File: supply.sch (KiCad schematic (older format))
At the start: 65 parts, among them IC1 TPS54561, J10 61300311121, J3 DC_SOCKET, U4 TPS65296, U5 TPS62823DLCT

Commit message: Replace 5R1 resistor and clean up
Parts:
- removed R41: R_5R1_1020, lpddr4-test-board-footprints:1020-res, symbol lpddr4-test-board:R_5R1_1020
- added R35: R_5R1_0402, antmicro-footprints:0402-res, symbol antmicroResistors0402:R_5R1_0402
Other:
- note added: "Decoupling"
- moved on the sheet: C165, C167, C170, C172, C174, C175, C178, C180, C182, C183, C27, C28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

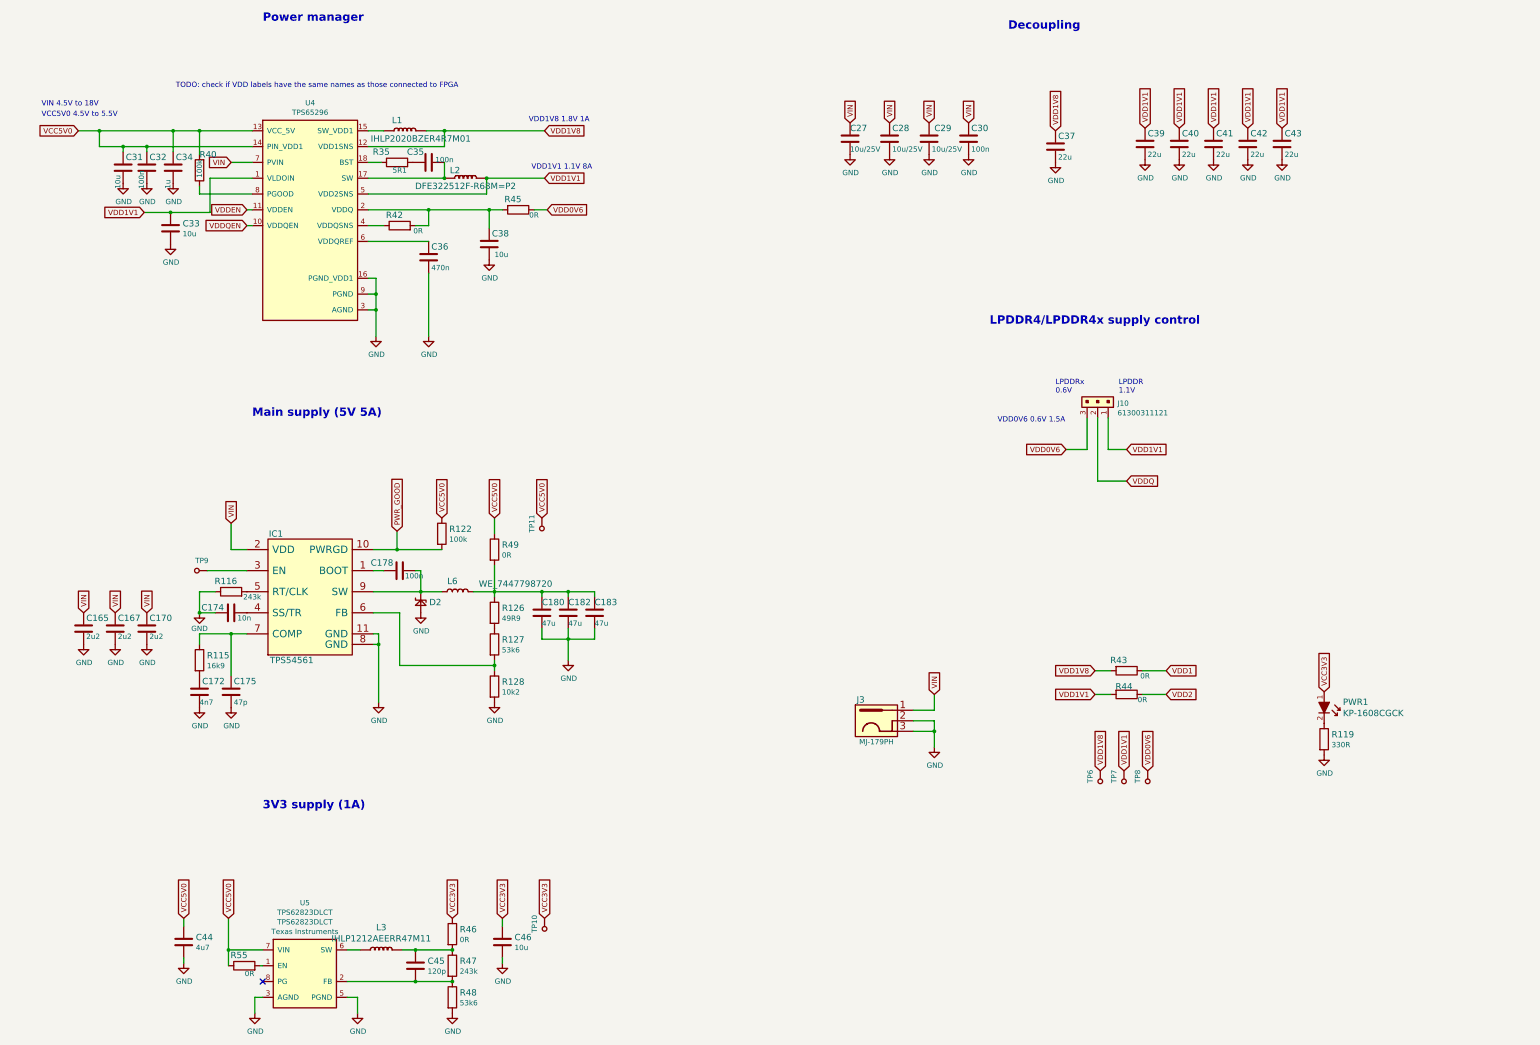
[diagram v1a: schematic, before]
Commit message: Clean up schematic
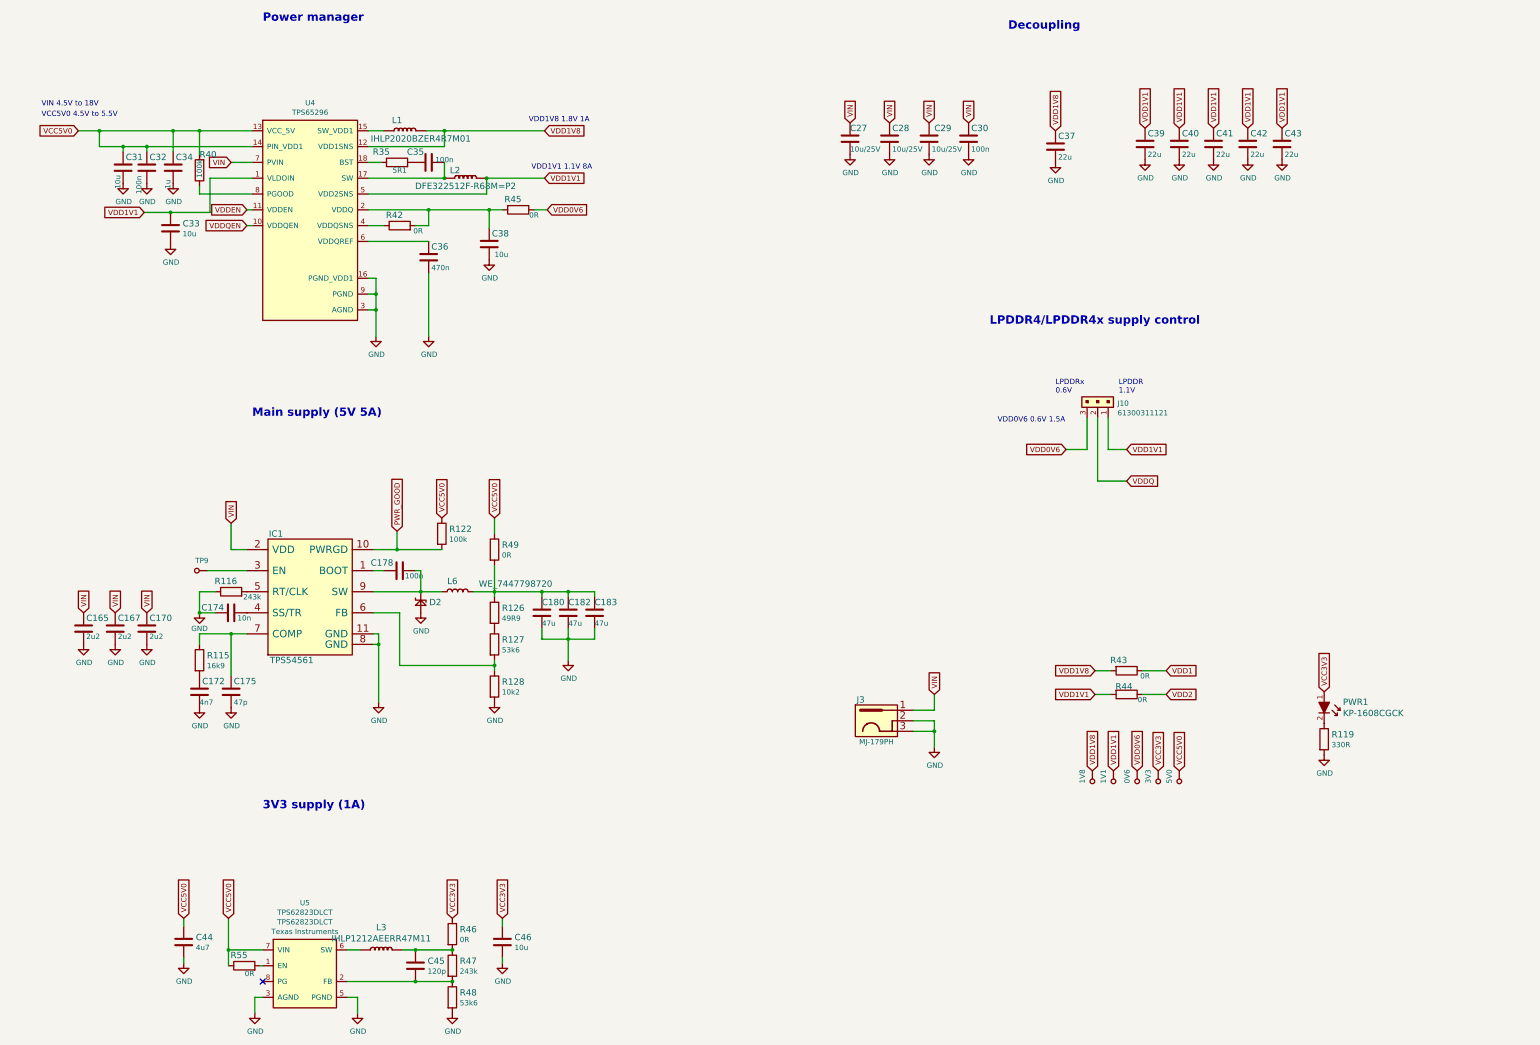
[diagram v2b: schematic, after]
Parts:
- renumbered TP8 to 0V6, TP7 to 1V1, TP6 to 1V8, TP10 to 3V3, TP11 to 5V0
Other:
- note removed: "TODO: check if VDD labels have the same names as those connected to FPGA"
- moved on the sheet: 0V6, 1V1, 1V8, 3V3, 5V0
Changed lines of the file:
@@
 F 4 "Walsin" H 2650 2750 60  0001 L CNN "Manufacturer"
 F 5 "0402X104K6R3CT" H 2650 2650 60  0001 L CNN "MPN"
-F 6 "100n" V 2400 2150 50  0000 L CNN "Val"
+F 6 "100n" V 2375 2100 50  0000 L CNN "Val"
 	1    2450 2350
 	1    0    0    -1
@@
 Wire Wire Line
 	4450 10225 4450 10375
-Text Notes 2725 1600 0    50   ~ 0
-TODO: check if VDD labels have the same names as those connected to FPGA
 $Comp
 L lpddr4-test-board:IHLP1212AEERR47M11 L3
@@
 	0    1    1    0
 $EndComp
-Text GLabel 6200 5675 1    50   Input ~ 0
+Text GLabel 12250 8075 1    50   Input ~ 0
 VCC5V0
 $Comp
-L lpddr4-test-board:TP_SMD1MM TP11
+L lpddr4-test-board:TP_SMD1MM 5V0
 U 1 1 60212554
-P 6200 5775
-F 0 "TP11" V 6105 5822 50  0000 C CNN
-F 1 "TP_SMD1MM" H 6200 5675 50  0001 C CNN
-F 2 "lpddr4-test-board-footprints:Testpoint_smd_1mm" H 6400 5975 60  0001 L CNN
-F 3 "" H 6400 6075 60  0001 L CNN
-	1    6200 5775
+P 12250 8175
+F 0 "5V0" V 12155 8222 50  0000 C CNN
+F 1 "TP_SMD1MM" H 12250 8075 50  0001 C CNN
+F 2 "lpddr4-test-board-footprints:Testpoint_smd_1mm" H 12450 8375 60  0001 L CNN
+F 3 "" H 12450 8475 60  0001 L CNN
+	1    12250 8175
 	1    0    0    -1
 $EndComp
@@
 Wire Wire Line
 	5825 9850 5825 9900
-Text GLabel 6225 9475 1    50   Input ~ 0
+Text GLabel 12050 8075 1    50   Input ~ 0
 VCC3V3
 $Comp
-L lpddr4-test-board:TP_SMD1MM TP10
+L lpddr4-test-board:TP_SMD1MM 3V3
 U 1 1 6026C4D0
-P 6225 9575
-F 0 "TP10" V 6130 9622 50  0000 C CNN
-F 1 "TP_SMD1MM" H 6225 9475 50  0001 C CNN
-F 2 "lpddr4-test-board-footprints:Testpoint_smd_1mm" H 6425 9775 60  0001 L CNN
-F 3 "" H 6425 9875 60  0001 L CNN
-	1    6225 9575
+P 12050 8175
+F 0 "3V3" V 11955 8222 50  0000 C CNN
+F 1 "TP_SMD1MM" H 12050 8075 50  0001 C CNN
+F 2 "lpddr4-test-board-footprints:Testpoint_smd_1mm" H 12250 8375 60  0001 L CNN
+F 3 "" H 12250 8475 60  0001 L CNN
+	1    12050 8175
 	1    0    0    -1
 $EndComp
@@
 	-1   0    0    1
 $EndComp
-Text GLabel 11950 8075 1    50   Input ~ 0
+Text GLabel 11850 8075 1    50   Input ~ 0
 VDD0V6
 $Comp
-L lpddr4-test-board:TP_SMD1MM TP6
+L lpddr4-test-board:TP_SMD1MM 1V8
 U 1 1 602C0646
-P 11500 8175
-F 0 "TP6" V 11405 8222 50  0000 C CNN
-F 1 "TP_SMD1MM" H 11500 8075 50  0001 C CNN
-F 2 "lpddr4-test-board-footprints:Testpoint_smd_1mm" H 11700 8375 60  0001 L CNN
-F 3 "" H 11700 8475 60  0001 L CNN
-	1    11500 8175
-	1    0    0    -1
-$EndComp
-$Comp
-L lpddr4-test-board:TP_SMD1MM TP7
+P 11425 8175
+F 0 "1V8" V 11330 8222 50  0000 C CNN
+F 1 "TP_SMD1MM" H 11425 8075 50  0001 C CNN
+F 2 "lpddr4-test-board-footprints:Testpoint_smd_1mm" H 11625 8375 60  0001 L CNN
+F 3 "" H 11625 8475 60  0001 L CNN
+	1    11425 8175
+	1    0    0    -1
+$EndComp
+$Comp
+L lpddr4-test-board:TP_SMD1MM 1V1
 U 1 1 602C252D
-P 11725 8175
-F 0 "TP7" V 11630 8222 50  0000 C CNN
-F 1 "TP_SMD1MM" H 11725 8075 50  0001 C CNN
-F 2 "lpddr4-test-board-footprints:Testpoint_smd_1mm" H 11925 8375 60  0001 L CNN
-F 3 "" H 11925 8475 60  0001 L CNN
-	1    11725 8175
-	1    0    0    -1
-$EndComp
-$Comp
-L lpddr4-test-board:TP_SMD1MM TP8
+P 11625 8175
+F 0 "1V1" V 11530 8222 50  0000 C CNN
+F 1 "TP_SMD1MM" H 11625 8075 50  0001 C CNN
+F 2 "lpddr4-test-board-footprints:Testpoint_smd_1mm" H 11825 8375 60  0001 L CNN
+F 3 "" H 11825 8475 60  0001 L CNN
+	1    11625 8175
+	1    0    0    -1
+$EndComp
+$Comp
+L lpddr4-test-board:TP_SMD1MM 0V6
 U 1 1 602C27EC
-P 11950 8175
-F 0 "TP8" V 11855 8222 50  0000 C CNN
-F 1 "TP_SMD1MM" H 11950 8075 50  0001 C CNN
-F 2 "lpddr4-test-board-footprints:Testpoint_smd_1mm" H 12150 8375 60  0001 L CNN
-F 3 "" H 12150 8475 60  0001 L CNN
-	1    11950 8175
+P 11850 8175
+F 0 "0V6" V 11755 8222 50  0000 C CNN
+F 1 "TP_SMD1MM" H 11850 8075 50  0001 C CNN
+F 2 "lpddr4-test-board-footprints:Testpoint_smd_1mm" H 12050 8375 60  0001 L CNN
+F 3 "" H 12050 8475 60  0001 L CNN
+	1    11850 8175
 	1    0    0    -1
 $EndComp
@@
 Wire Wire Line
 	5675 2450 6225 2450
-Text GLabel 11725 8075 1    50   Input ~ 0
+Text GLabel 11625 8075 1    50   Input ~ 0
 VDD1V1
-Text GLabel 11500 8075 1    50   Input ~ 0
+Text GLabel 11425 8075 1    50   Input ~ 0
 VDD1V8
 Text GLabel 11450 7125 0    50   Input ~ 0

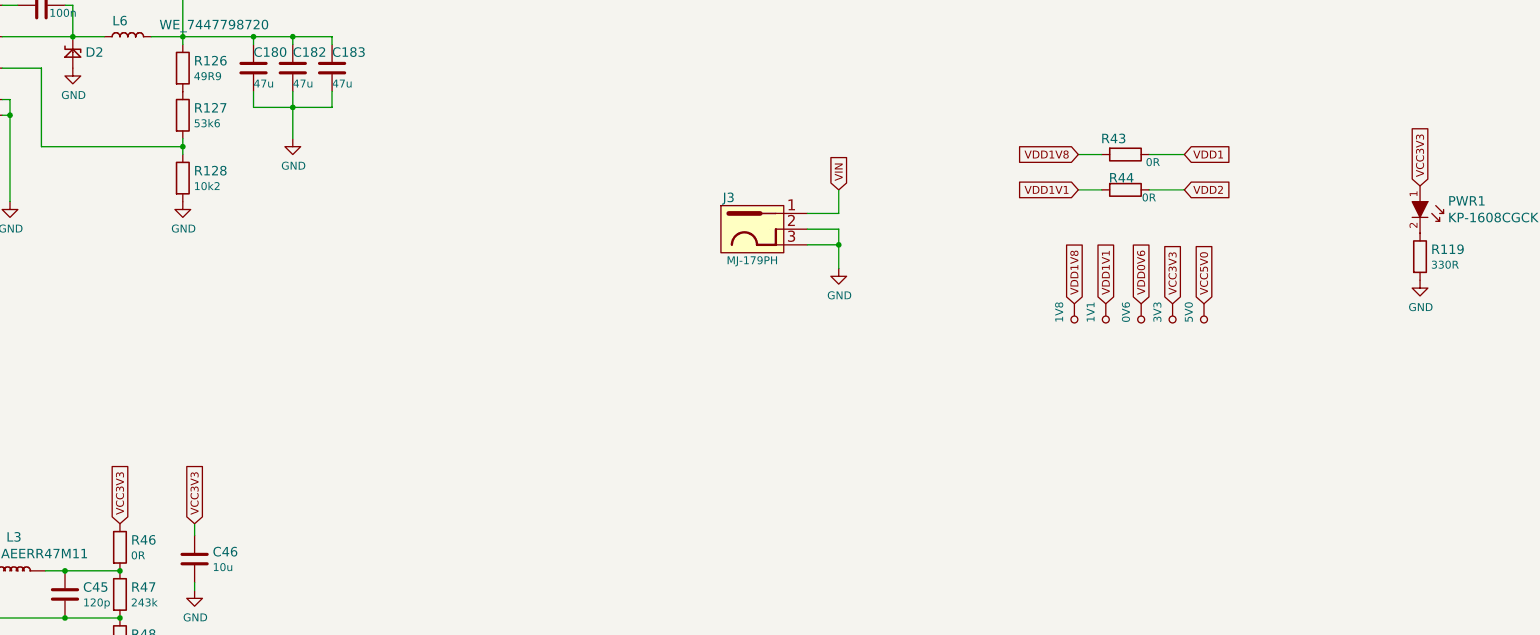
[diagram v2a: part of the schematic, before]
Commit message: Replace VCC3V3 with 3V3_SYS
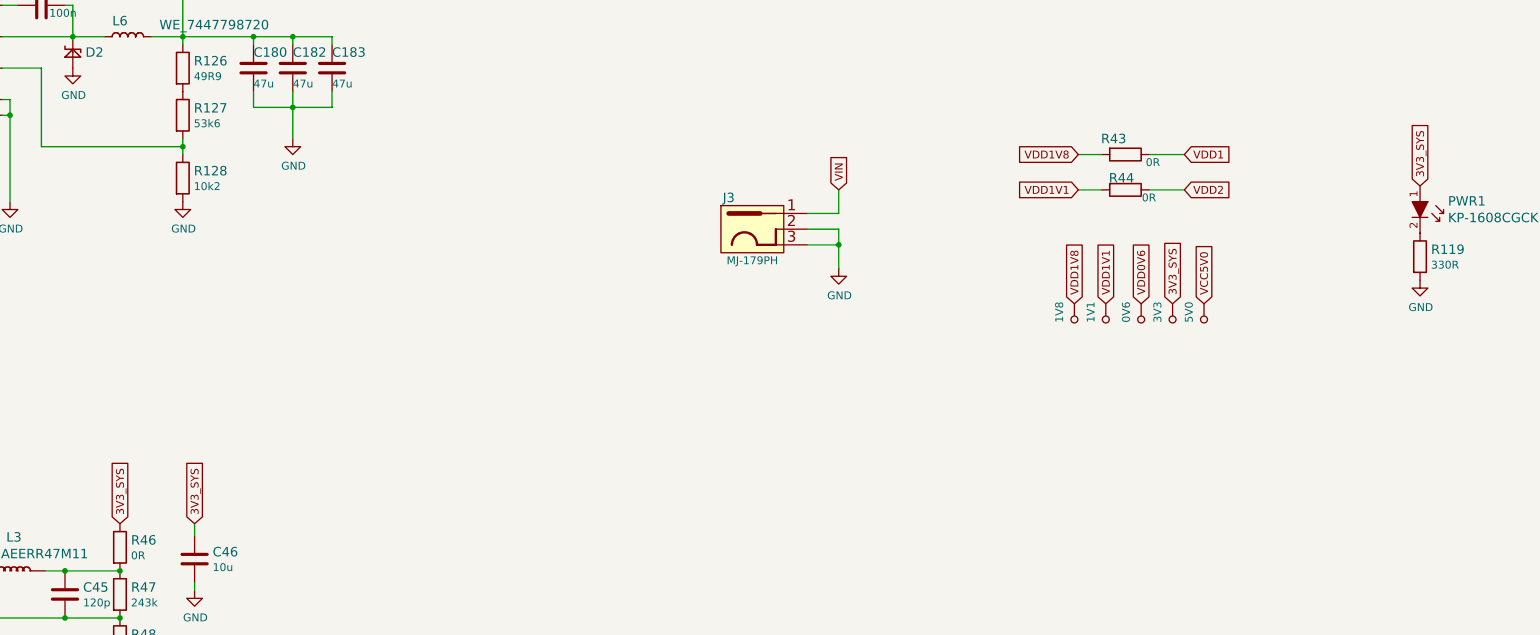
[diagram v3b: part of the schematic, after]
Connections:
- net VCC3V3 renamed 3V3_SYS
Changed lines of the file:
@@
 $EndComp
 Text GLabel 13625 7325 1    50   Input ~ 0
-VCC3V3
+3V3_SYS
 $Comp
 L lpddr4-test-board:R_330R_0402 R119
@@
 $EndComp
 Text GLabel 5825 9475 1    50   Input ~ 0
-VCC3V3
+3V3_SYS
 $Comp
 L lpddr4-test-board:GND #PWR0166
@@
 $EndComp
 Text GLabel 5350 9475 1    50   Input ~ 0
-VCC3V3
+3V3_SYS
 Text Notes 3550 8450 0    79   ~ 16
 3V3 supply (1A)
@@
 	5825 9850 5825 9900
 Text GLabel 12050 8075 1    50   Input ~ 0
-VCC3V3
+3V3_SYS
 $Comp
 L lpddr4-test-board:TP_SMD1MM 3V3

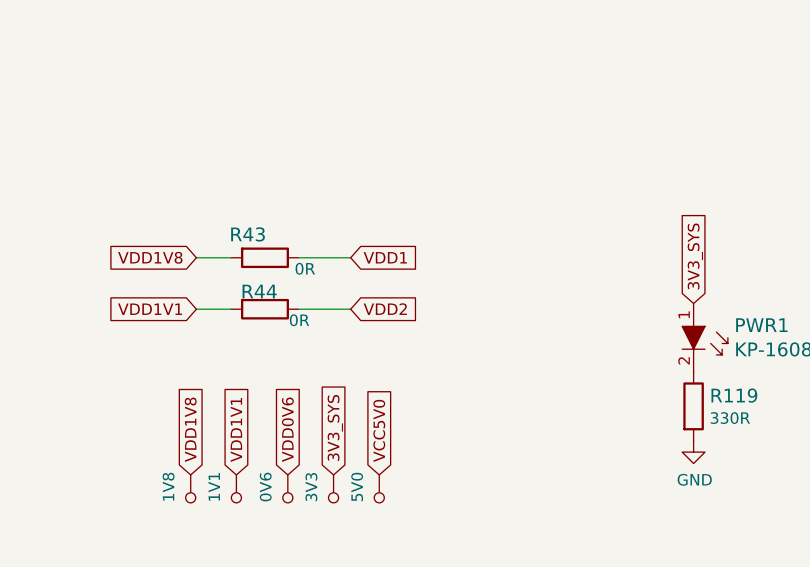
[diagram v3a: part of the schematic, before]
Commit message: Introduce unified 1V1_SYS 1V8_SYS 3V3_SYS
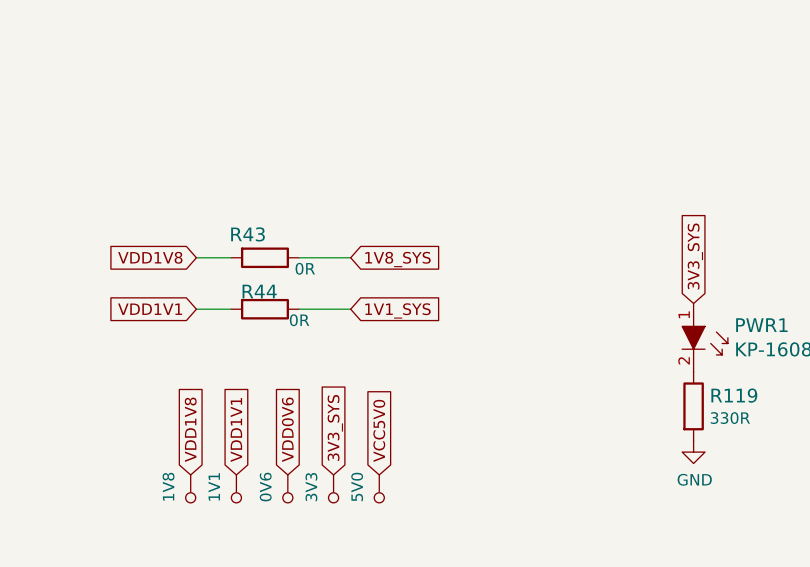
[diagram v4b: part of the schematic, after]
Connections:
- net VDD1 renamed 1V8_SYS
- net VDD2 renamed 1V1_SYS
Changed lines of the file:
@@
 VDD1V1
 Text GLabel 12125 7125 2    50   Input ~ 0
-VDD1
+1V8_SYS
 Text GLabel 12125 7350 2    50   Input ~ 0
-VDD2
+1V1_SYS
 Wire Wire Line
 	11450 7125 11600 7125
